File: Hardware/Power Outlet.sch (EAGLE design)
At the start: 28 parts, among them IC1 ATMega 328p-pu, IC2 ULN2003AD, K1 G5LE, K2 G5LE, Q1 16MHz

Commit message: updated LED values/names
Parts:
- LED1: value HEAT -> OUT2
- LED2: value WATER -> OUT1
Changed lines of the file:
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@@
 <?xml version="1.0" encoding="utf-8"?>
 <!DOCTYPE eagle SYSTEM "eagle.dtd">
-<eagle version="6.5.0">
+<eagle version="6.4">
 <drawing>
 <settings>
@@
 <part name="S1" library="switch-omron" deviceset="40-XX" device="" value="OUT1_SW"/>
 <part name="S2" library="switch-omron" deviceset="40-XX" device="" value="OUT2_SW"/>
-<part name="LED1" library="led" deviceset="LED" device="5MM" value="HEAT"/>
-<part name="LED2" library="led" deviceset="LED" device="5MM" value="WATER"/>
+<part name="LED1" library="led" deviceset="LED" device="5MM" value="OUT2"/>
+<part name="LED2" library="led" deviceset="LED" device="5MM" value="OUT1"/>
 <part name="IC1" library="ic-package" deviceset="DIL28" device="-4" value="ATMega 328p-pu"/>
 <part name="Q1" library="crystal" deviceset="CRYSTAL" device="HC49S" value="16MHz"/>

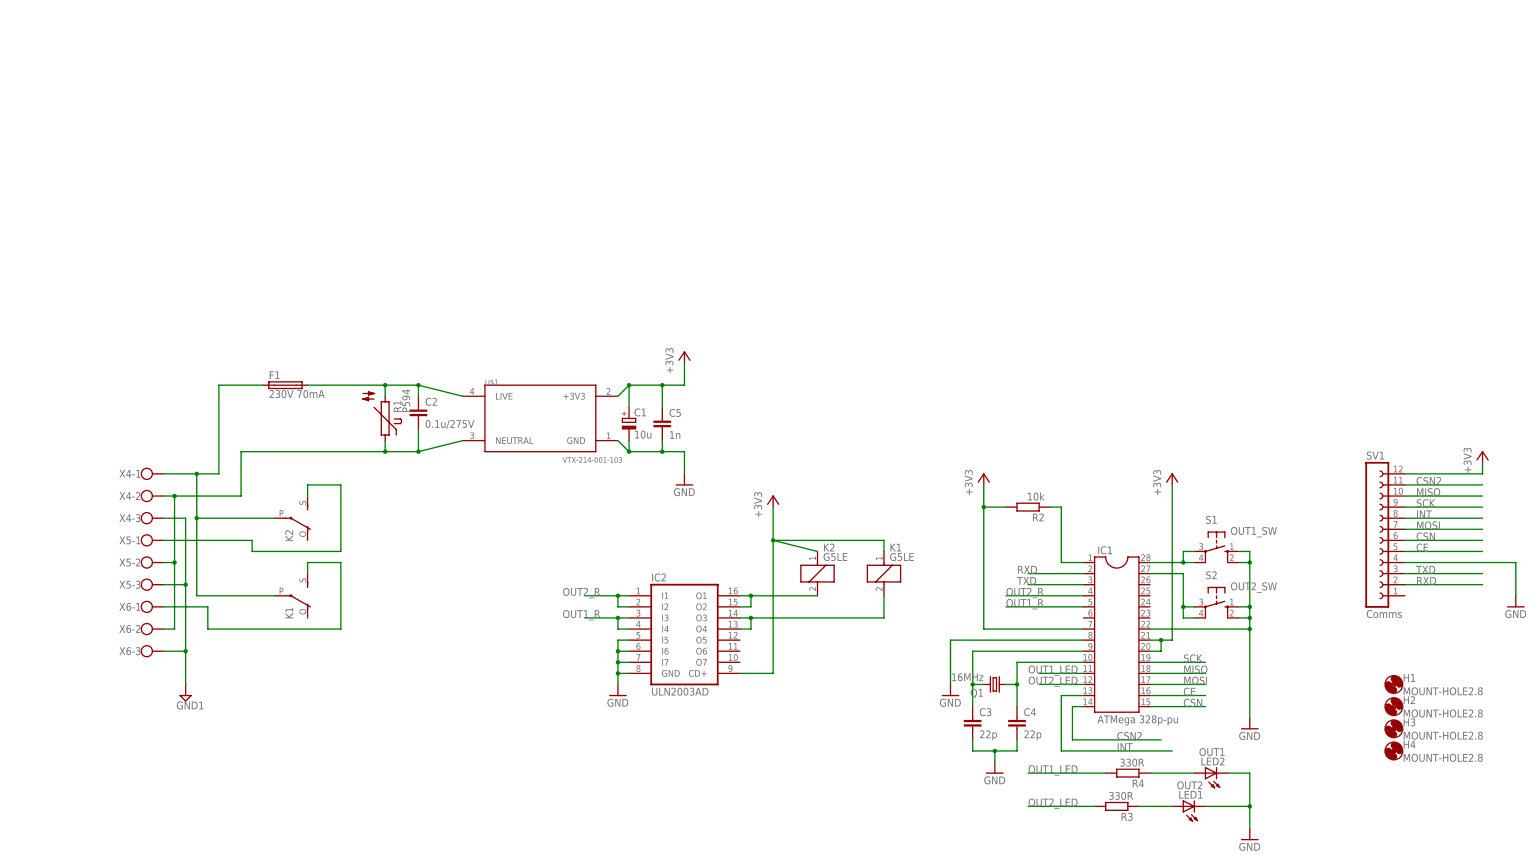
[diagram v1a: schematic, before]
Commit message: initial mock up of board. added optocouplers to help increase isolation from mains
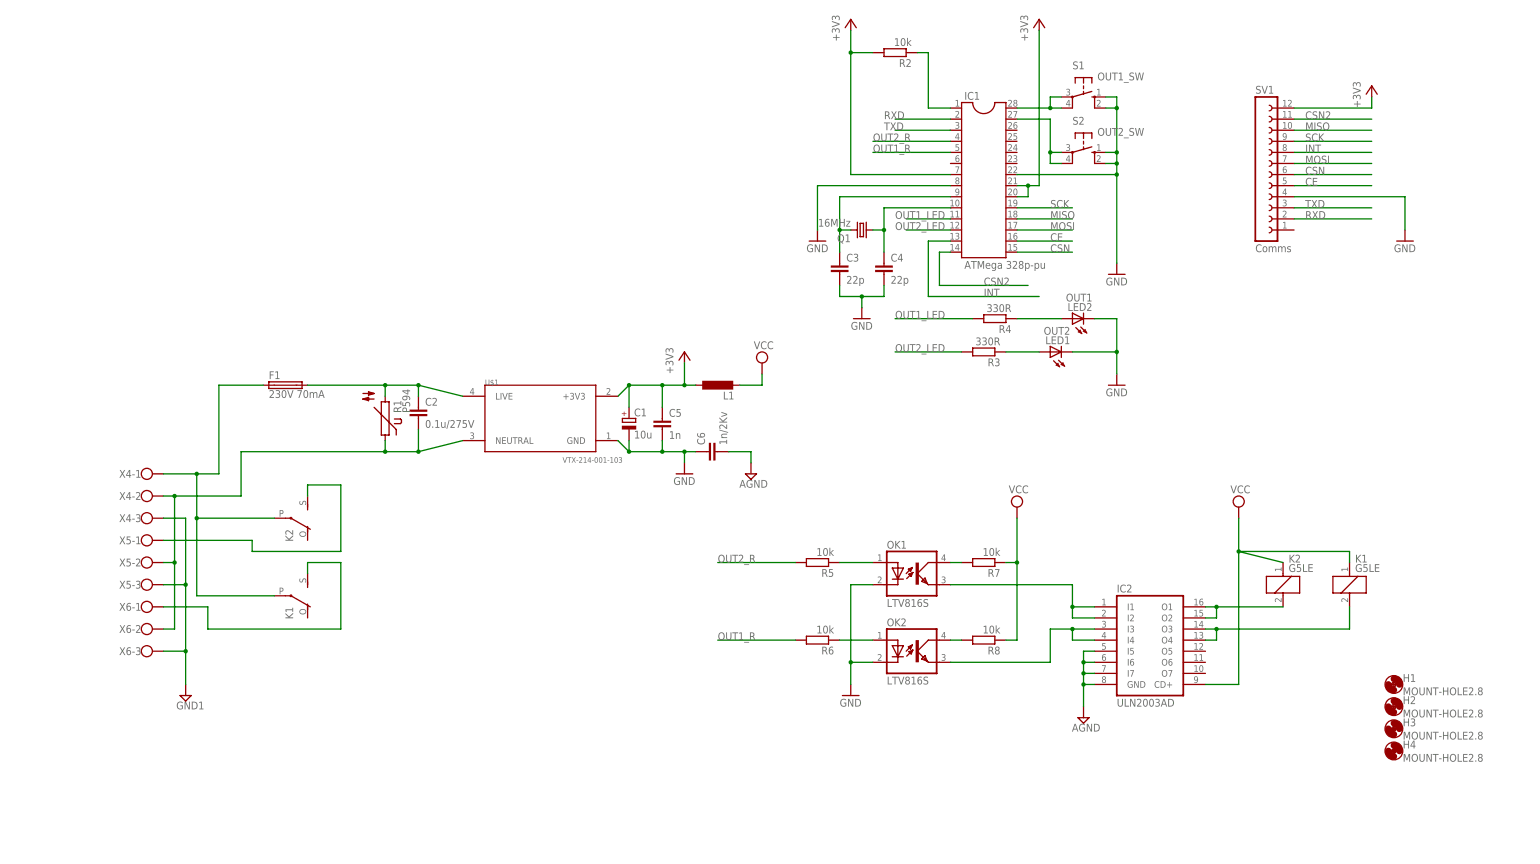
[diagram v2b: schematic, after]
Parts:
- added C6: 1n/2Kv, rcl:C-EUC1206K
- added L1: (no value), rcl:L-EUL3225P
- added OK1, OK2: LTV816S, optocoupler:LTV816S
- added R5, R6, R7, R8: 10k, rcl:R-EU_R1206W
- C1: device rcl:CPOL-EU153CLV-1010 -> rcl:CPOL-EUE2,5-6E
- C2: device rcl:C-EU025-025X050 -> rcl:C-EU050-030X075
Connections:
- new net AGND: C6.2, IC2.GND, IC2.I5, IC2.I6, IC2.I7
- new net N$15: OK1.A, R5.1
- new net N$16: OK2.A, R6.1
- new net N$17: IC2.I1, IC2.I2, OK1.EMIT
- new net N$18: IC2.I3, IC2.I4, OK2.EMIT
- new net N$19: OK1.COL, R7.2
- new net N$20: OK2.COL, R8.2
- new net VCC: IC2.CD+, K11.1, K21.1, L1.2, R7.1, R8.1
- net +3V3: now also L1.1; no longer IC2.CD+, K11.1, K21.1
- net GND: now also C6.1, OK1.C, OK2.C; no longer IC2.GND, IC2.I5, IC2.I6, IC2.I7
- net OUT1_R: now also R6.2; no longer IC2.I3, IC2.I4
- net OUT2_R: now also R5.2; no longer IC2.I1, IC2.I2
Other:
- moved on the sheet: C3, C4, IC1, IC2, K1, K2, LED1, LED2, Q1, R2, R3, R4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

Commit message: Finilised Rev A. Power Outlet Board
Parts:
- removed X4, X5, X6: (no value), con-wago-500:W237-103
- added X1: VIN, con-wago-500:W237-102
- added X2: VOUT2, con-wago-500:W237-102
- added X3: VOUT1, con-wago-500:W237-102
- added X7: EARTH, con-wago-500:W237-103
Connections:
- net GND1: now also X7-1.KL, X7-2.KL, X7-3.KL; no longer X4-3.KL, X5-3.KL, X6-3.KL
- net N$1: now also X1-1.KL; no longer X4-1.KL
- net N$11: now also X2-1.KL; no longer X5-1.KL
- net N$14: now also X3-1.KL; no longer X6-1.KL
- net N$3: now also X1-2.KL, X2-2.KL, X3-2.KL; no longer X4-2.KL, X5-2.KL, X6-2.KL
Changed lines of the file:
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@@
 <part name="H3" library="holes" deviceset="MOUNT-HOLE" device="2.8"/>
 <part name="H4" library="holes" deviceset="MOUNT-HOLE" device="2.8"/>
-<part name="X4" library="con-wago-500" deviceset="W237-103" device=""/>
-<part name="X5" library="con-wago-500" deviceset="W237-103" device=""/>
-<part name="X6" library="con-wago-500" deviceset="W237-103" device=""/>
-<part name="EARTH" library="supply2" deviceset="GND1" device=""/>
 <part name="OK1" library="optocoupler" deviceset="LTV816" device="S"/>
 <part name="OK2" library="optocoupler" deviceset="LTV816" device="S"/>
@@
 <part name="R7" library="rcl" deviceset="R-EU_" device="R1206W" value="10k"/>
 <part name="R8" library="rcl" deviceset="R-EU_" device="R1206W" value="10k"/>
+<part name="X1" library="con-wago-500" deviceset="W237-102" device="" value="VIN"/>
+<part name="X2" library="con-wago-500" deviceset="W237-102" device="" value="VOUT2"/>
+<part name="X3" library="con-wago-500" deviceset="W237-102" device="" value="VOUT1"/>
+<part name="X7" library="con-wago-500" deviceset="W237-103" device="" value="EARTH"/>
+<part name="EARTH1" library="supply2" deviceset="GND1" device=""/>
 </parts>
 <sheets>
@@
 <instance part="H3" gate="G$1" x="228.6" y="-2.54"/>
 <instance part="H4" gate="G$1" x="228.6" y="-7.62"/>
-<instance part="X4" gate="-1" x="-58.42" y="55.88"/>
-<instance part="X4" gate="-2" x="-58.42" y="50.8"/>
-<instance part="X4" gate="-3" x="-58.42" y="45.72"/>
-<instance part="X5" gate="-1" x="-58.42" y="40.64"/>
-<instance part="X5" gate="-2" x="-58.42" y="35.56"/>
-<instance part="X5" gate="-3" x="-58.42" y="30.48"/>
-<instance part="X6" gate="-1" x="-58.42" y="25.4"/>
-<instance part="X6" gate="-2" x="-58.42" y="20.32"/>
-<instance part="X6" gate="-3" x="-58.42" y="15.24"/>
-<instance part="EARTH" gate="G$1" x="-48.26" y="5.08"/>
 <instance part="OK1" gate="G$1" x="119.38" y="33.02"/>
 <instance part="OK2" gate="G$1" x="119.38" y="15.24"/>
@@
 <instance part="R7" gate="G$1" x="134.62" y="35.56" rot="R180"/>
 <instance part="R8" gate="G$1" x="134.62" y="17.78" rot="R180"/>
+<instance part="X1" gate="-1" x="-78.74" y="50.8"/>
+<instance part="X1" gate="-2" x="-78.74" y="45.72"/>
+<instance part="X2" gate="-1" x="-78.74" y="38.1"/>
+<instance part="X2" gate="-2" x="-78.74" y="33.02"/>
+<instance part="X3" gate="-1" x="-78.74" y="22.86"/>
+<instance part="X3" gate="-2" x="-78.74" y="17.78"/>
+<instance part="X7" gate="-1" x="-81.28" y="7.62"/>
+<instance part="X7" gate="-2" x="-81.28" y="2.54"/>
+<instance part="X7" gate="-3" x="-81.28" y="-2.54"/>
+<instance part="EARTH1" gate="G$1" x="-71.12" y="-10.16"/>
 </instances>
 <busses>
@@
 <pinref part="R1" gate="1" pin="1"/>
 <wire x1="-2.54" y1="63.5" x2="-2.54" y2="60.96" width="0.1524" layer="91"/>
-<pinref part="X4" gate="-2" pin="KL"/>
-<wire x1="-53.34" y1="50.8" x2="-50.8" y2="50.8" width="0.1524" layer="91"/>
-<wire x1="-50.8" y1="50.8" x2="-35.56" y2="50.8" width="0.1524" layer="91"/>
+<wire x1="-68.58" y1="50.8" x2="-35.56" y2="50.8" width="0.1524" layer="91"/>
 <wire x1="-35.56" y1="50.8" x2="-35.56" y2="60.96" width="0.1524" layer="91"/>
 <wire x1="-35.56" y1="60.96" x2="-2.54" y2="60.96" width="0.1524" layer="91"/>
 <junction x="-2.54" y="60.96"/>
-<pinref part="X5" gate="-2" pin="KL"/>
-<wire x1="-53.34" y1="35.56" x2="-50.8" y2="35.56" width="0.1524" layer="91"/>
-<wire x1="-50.8" y1="35.56" x2="-50.8" y2="50.8" width="0.1524" layer="91"/>
-<pinref part="X6" gate="-2" pin="KL"/>
-<wire x1="-53.34" y1="20.32" x2="-50.8" y2="20.32" width="0.1524" layer="91"/>
-<wire x1="-50.8" y1="20.32" x2="-50.8" y2="35.56" width="0.1524" layer="91"/>
-<junction x="-50.8" y="35.56"/>
-<junction x="-50.8" y="50.8"/>
+<pinref part="X3" gate="-2" pin="KL"/>
+<wire x1="-73.66" y1="17.78" x2="-68.58" y2="17.78" width="0.1524" layer="91"/>
+<pinref part="X2" gate="-2" pin="KL"/>
+<wire x1="-73.66" y1="33.02" x2="-68.58" y2="33.02" width="0.1524" layer="91"/>
+<wire x1="-68.58" y1="33.02" x2="-68.58" y2="17.78" width="0.1524" layer="91"/>
+<pinref part="X1" gate="-2" pin="KL"/>
+<wire x1="-73.66" y1="45.72" x2="-68.58" y2="45.72" width="0.1524" layer="91"/>
+<wire x1="-68.58" y1="45.72" x2="-68.58" y2="33.02" width="0.1524" layer="91"/>
+<junction x="-68.58" y="33.02"/>
+<wire x1="-68.58" y1="45.72" x2="-68.58" y2="50.8" width="0.1524" layer="91"/>
+<junction x="-68.58" y="45.72"/>
 </segment>
 </net>
@@
 <wire x1="-30.48" y1="76.2" x2="-40.64" y2="76.2" width="0.1524" layer="91"/>
 <wire x1="-40.64" y1="76.2" x2="-40.64" y2="55.88" width="0.1524" layer="91"/>
-<pinref part="X4" gate="-1" pin="KL"/>
 <wire x1="-40.64" y1="55.88" x2="-45.72" y2="55.88" width="0.1524" layer="91"/>
 <pinref part="K2" gate="2" pin="P"/>
-<wire x1="-45.72" y1="55.88" x2="-53.34" y2="55.88" width="0.1524" layer="91"/>
 <wire x1="-27.94" y1="45.72" x2="-45.72" y2="45.72" width="0.1524" layer="91"/>
 <wire x1="-45.72" y1="45.72" x2="-45.72" y2="55.88" width="0.1524" layer="91"/>
@@
 <junction x="-45.72" y="45.72"/>
 <junction x="-45.72" y="55.88"/>
+<pinref part="X1" gate="-1" pin="KL"/>
+<wire x1="-73.66" y1="50.8" x2="-73.66" y2="55.88" width="0.1524" layer="91"/>
+<wire x1="-73.66" y1="55.88" x2="-45.72" y2="55.88" width="0.1524" layer="91"/>
 </segment>
 </net>
 <net name="GND1" class="0">
 <segment>
-<pinref part="X4" gate="-3" pin="KL"/>
-<wire x1="-53.34" y1="45.72" x2="-48.26" y2="45.72" width="0.1524" layer="91"/>
-<pinref part="X6" gate="-3" pin="KL"/>
-<wire x1="-48.26" y1="45.72" x2="-48.26" y2="30.48" width="0.1524" layer="91"/>
-<wire x1="-48.26" y1="30.48" x2="-48.26" y2="15.24" width="0.1524" layer="91"/>
-<wire x1="-48.26" y1="15.24" x2="-48.26" y2="7.62" width="0.1524" layer="91"/>
-<wire x1="-53.34" y1="15.24" x2="-48.26" y2="15.24" width="0.1524" layer="91"/>
-<junction x="-48.26" y="15.24"/>
-<pinref part="EARTH" gate="G$1" pin="GND1"/>
-<pinref part="X5" gate="-3" pin="KL"/>
-<wire x1="-53.34" y1="30.48" x2="-48.26" y2="30.48" width="0.1524" layer="91"/>
-<junction x="-48.26" y="30.48"/>
+<pinref part="EARTH1" gate="G$1" pin="GND1"/>
+<pinref part="X7" gate="-3" pin="KL"/>
+<wire x1="-71.12" y1="-7.62" x2="-71.12" y2="-2.54" width="0.1524" layer="91"/>
+<wire x1="-71.12" y1="-2.54" x2="-76.2" y2="-2.54" width="0.1524" layer="91"/>
+<pinref part="X7" gate="-2" pin="KL"/>
+<wire x1="-76.2" y1="2.54" x2="-71.12" y2="2.54" width="0.1524" layer="91"/>
+<wire x1="-71.12" y1="2.54" x2="-71.12" y2="-2.54" width="0.1524" layer="91"/>
+<pinref part="X7" gate="-1" pin="KL"/>
+<wire x1="-76.2" y1="7.62" x2="-71.12" y2="7.62" width="0.1524" layer="91"/>
+<wire x1="-71.12" y1="7.62" x2="-71.12" y2="2.54" width="0.1524" layer="91"/>
+<junction x="-71.12" y="2.54"/>
+<junction x="-71.12" y="-2.54"/>
 </segment>
 </net>
@@
 <wire x1="-20.32" y1="53.34" x2="-12.7" y2="53.34" width="0.1524" layer="91"/>
 <wire x1="-12.7" y1="53.34" x2="-12.7" y2="38.1" width="0.1524" layer="91"/>
-<wire x1="-12.7" y1="38.1" x2="-33.02" y2="38.1" width="0.1524" layer="91"/>
-<wire x1="-33.02" y1="38.1" x2="-33.02" y2="40.64" width="0.1524" layer="91"/>
-<pinref part="X5" gate="-1" pin="KL"/>
-<wire x1="-33.02" y1="40.64" x2="-53.34" y2="40.64" width="0.1524" layer="91"/>
+<wire x1="-12.7" y1="38.1" x2="-38.1" y2="38.1" width="0.1524" layer="91"/>
+<pinref part="X2" gate="-1" pin="KL"/>
+<wire x1="-73.66" y1="38.1" x2="-38.1" y2="38.1" width="0.1524" layer="91"/>
 </segment>
 </net>
@@
 <wire x1="-20.32" y1="35.56" x2="-12.7" y2="35.56" width="0.1524" layer="91"/>
 <wire x1="-12.7" y1="35.56" x2="-12.7" y2="20.32" width="0.1524" layer="91"/>
-<wire x1="-12.7" y1="20.32" x2="-43.18" y2="20.32" width="0.1524" layer="91"/>
-<wire x1="-43.18" y1="20.32" x2="-43.18" y2="25.4" width="0.1524" layer="91"/>
-<pinref part="X6" gate="-1" pin="KL"/>
-<wire x1="-43.18" y1="25.4" x2="-53.34" y2="25.4" width="0.1524" layer="91"/>
-</segment>
-</net>
+<wire x1="-12.7" y1="20.32" x2="-45.72" y2="20.32" width="0.1524" layer="91"/>
+<wire x1="-45.72" y1="20.32" x2="-45.72" y2="22.86" width="0.1524" layer="91"/>
+<wire x1="-45.72" y1="22.86" x2="-73.66" y2="22.86" width="0.1524" layer="91"/>
+<pinref part="X3" gate="-1" pin="KL"/>
+</segment>
+</net>
